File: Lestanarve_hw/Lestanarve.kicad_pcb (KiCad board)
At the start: 2 copper layers, 39 x 19.2 mm, 0 parts

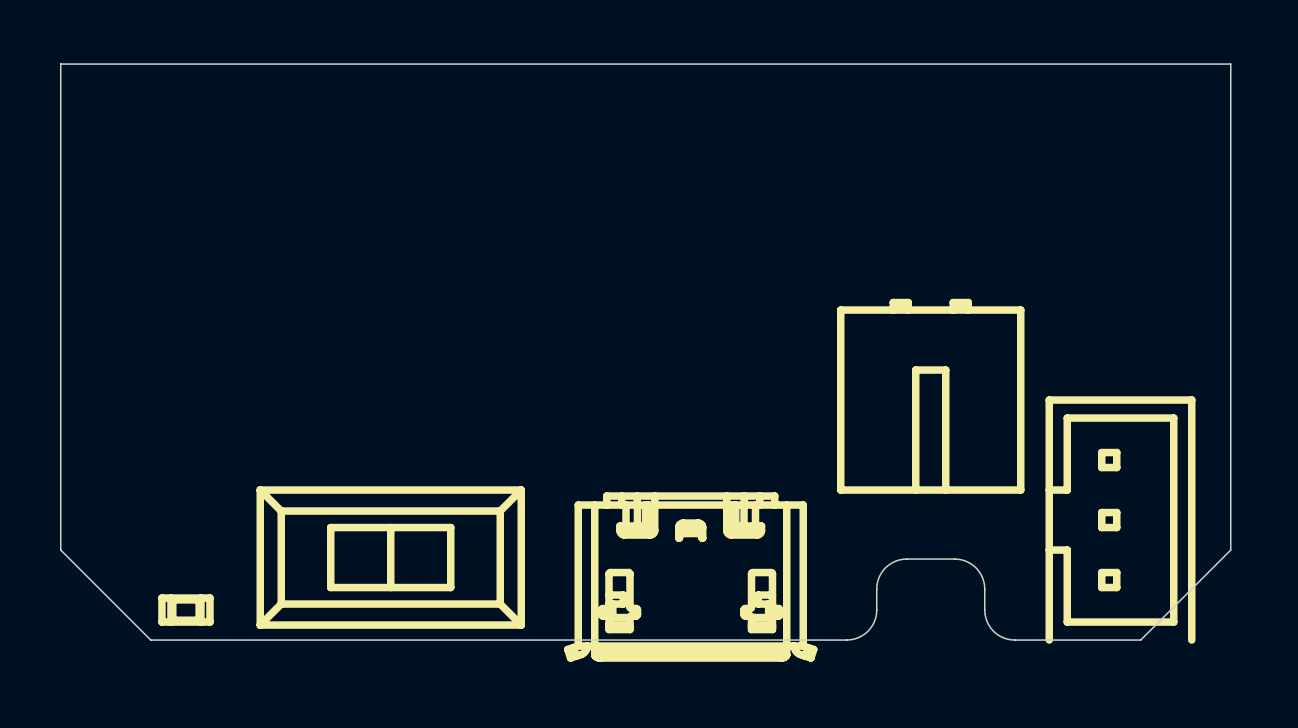
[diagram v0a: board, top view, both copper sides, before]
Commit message: + UART works
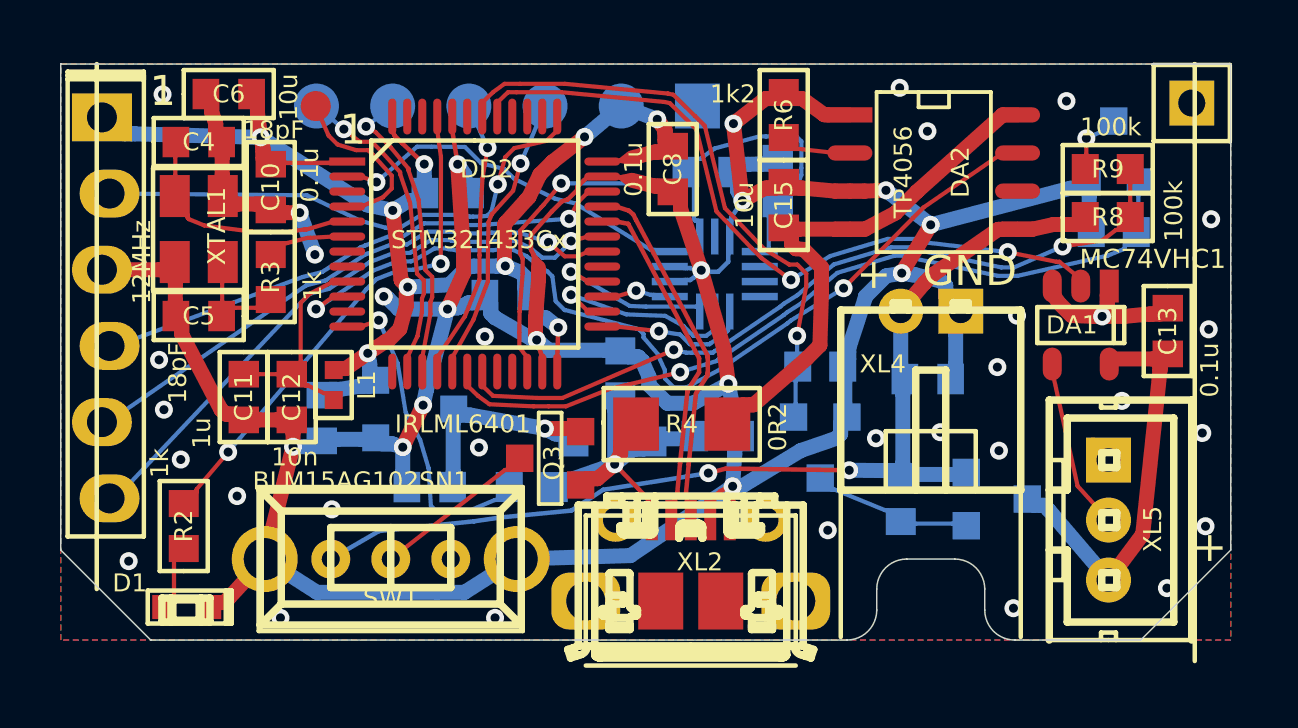
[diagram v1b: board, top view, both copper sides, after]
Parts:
- added C1: 10n, Capacitors:CAP_0603_Silks, B.Cu at (141.4, 92.5)
- added C10: 0.1u, Capacitors:CAP_0603_Silks, F.Cu at (126.5, 84.2)
- added C11: 1u, Capacitors:CAP_0603_Silks, F.Cu at (125.6, 91.2)
- added C12: 10n, Capacitors:CAP_0603_Silks, F.Cu at (127.2, 91.2)
- added C13: 0.1u, Capacitors:CAP_0603_Silks, F.Cu at (156.4, 89.0)
- added C15: 10u, Capacitors:CAP_0603_Silks, F.Cu at (143.6, 84.8)
- added C16: 10u, Capacitors:CAP_0603_Silks, B.Cu at (148.4, 90.6)
- added C17: 1u, Capacitors:CAP_0603_Silks, B.Cu at (131.8, 94.2)
- added C18: 1u, Capacitors:CAP_0603_Silks, B.Cu at (128.2, 91.9)
- added C2: 0.1u, Capacitors:CAP_0603_Silks, B.Cu at (143.4, 84.0)
- added C3: 0.1u, Capacitors:CAP_0603_Silks, B.Cu at (141.1, 83.7)
- added C4: 18pF, Capacitors:CAP_0603_Silks, F.Cu at (124.1, 82.7)
- added C5: 18pF, Capacitors:CAP_0603_Silks, F.Cu at (124.1, 88.5)
- added C6: 10u, Capacitors:CAP_0603_Silks, F.Cu at (125.1, 81.1)
- added C7: 0.1u, Capacitors:CAP_0603_Silks, B.Cu at (134.4, 87.8)
- added C8: 0.1u, Capacitors:CAP_0603_Silks, F.Cu at (139.9, 83.6)
- added C9: 0.1u, Capacitors:CAP_0603_Silks, B.Cu at (132.4, 84.4)
- added D1: LED, LEDs:LED_0603_ch, F.Cu at (123.7, 98.2)
- added D2: PMEG2020, Diodes:SOD323, B.Cu at (137.9, 92.7)
- added DA1: MC74VHC1, SOT:SOT23-5, F.Cu at (153.5, 88.8)
- added DA2: TP4056, SO_DIL_TSSOP:SO8_150MIL, F.Cu at (148.6, 83.7)
- added DA3: MCP1700, SOT:SOT23-3A, B.Cu at (131.3, 91.6)
- added DD1: LSM6DS3, LGA:14_3x2d5_p0d5, B.Cu at (141.3, 87.1)
- added DD2: STM32L433Cx, LQFP_TQFP:LQFP48, F.Cu at (133.3, 86.1)
- added L1: BLM15AG102SN1, Inductors:IND_0402, F.Cu at (128.6, 90.8)
- added Q1: IRLML6401, SOT:SOT23-3, B.Cu at (150.7, 94.6)
- added Q2: 2N7002, SOT:SOT23-3, B.Cu at (144.8, 92.9)
- added Q3: IRLML6401, SOT:SOT23-3, F.Cu at (135.8, 93.2)
- added Q4: 2N7002, SOT:SOT23-3, B.Cu at (154.6, 83.0)
- added R1: 1k, Resistors:RES_0603, B.Cu at (135.2, 94.2)
- added R10: 100k, Resistors:RES_0603, B.Cu at (154.6, 85.7)
- added R11: 10k, Resistors:RES_0603, B.Cu at (138.2, 90.4)
- added R2: 1k, Resistors:RES_0603, F.Cu at (123.6, 95.5)
- added R3: 1k, Resistors:RES_0603, F.Cu at (126.5, 87.2)
- added R4: 0R2, Resistors:RES_1206, F.Cu at (140.2, 92.1)
- added R5: 10k, Resistors:RES_0603, B.Cu at (147.5, 94.6)
- added R6: 1k2, Resistors:RES_0603, F.Cu at (143.6, 81.8)
- added R7: 100k, Resistors:RES_0603, B.Cu at (144.8, 90.2)
- added R8: 100k, Resistors:RES_0603, F.Cu at (154.4, 85.2)
- added R9: 100k, Resistors:RES_0603, F.Cu at (154.4, 83.6)
- added SW1: SWITCH, BtnsSwitches:SW_SS-1P2T_Housing, F.Cu at (130.5, 96.6)
- added TP1: TESTPOINT, PCB:TESTPOINT_1MM, F.Cu at (128.0, 81.5)
- added XL1: CONN_6, Connectors:PLS-6_LOCK, F.Cu at (121.0, 81.9)
- added XL2: USB_MICRO, Connectors:USBmicro_MOLEX_1050170001, F.Cu at (140.5, 99.5)
- added XL3: CONN_6, Connectors:PLS-6-NoHole, B.Cu at (140.7, 81.5)
- added XL4: CONN_2, Connectors:WB-02R(MW-2MR), F.Cu at (148.5, 88.3)
- added XL5: CONN_3, Connectors:WB-03(MW-3M), F.Cu at (154.4, 95.3)
- added XL6: CONN_1, Connectors:PLS-1Square, F.Cu at (157.2, 81.4)
- added XTAL1: 12MHz, Quartz:03225C4, F.Cu at (124.1, 85.6)
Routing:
- net GND: track 0.00 -> 152.4 mm, vias 0 -> 45
- net +3v3: track 0.00 -> 50.2 mm, vias 0 -> 9
- net +BATT: track 0.00 -> 34.7 mm, vias 0 -> 2
- net /IS_CHARGING: track 0.00 -> 30.2 mm, vias 0 -> 2
- net /ADC_BAT_EN: track 0.00 -> 26.5 mm, vias 0 -> 1
- net /ADC_BAT: track 0.00 -> 25.8 mm, vias 0 -> 2
- net /NPX1_CTRL: track 0.00 -> 24.3 mm, vias 0 -> 2
- net /ACC_PWR: track 0.00 -> 22.2 mm, vias 0 -> 1
- net /UART_RX: track 0.00 -> 20.3 mm, vias 0 -> 1
- net /NPX_PWR_EN: track 0.00 -> 19.8 mm, vias 0 -> 1
- net /UART_TX: track 0.00 -> 18.8 mm, vias 0 -> 1
- net /5V_MID: track 0.00 -> 17.9 mm
- net /SWDIO: track 0.00 -> 17.8 mm, vias 0 -> 1
- net /SWCLK: track 0.00 -> 17.5 mm, vias 0 -> 1
- net Net-(DD2-Pad45): track 0.00 -> 17.0 mm, vias 0 -> 2
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- added copper zone on B.Cu, net GND
- added copper zone on F.Cu, net GND
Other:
- rule pad_to_mask_clearance: 0 -> 0.06
- board text added: "+"
- board text added: "D"
- board text added: "GND"
